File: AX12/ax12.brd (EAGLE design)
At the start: 36.8 x 40.3 mm, 14 parts

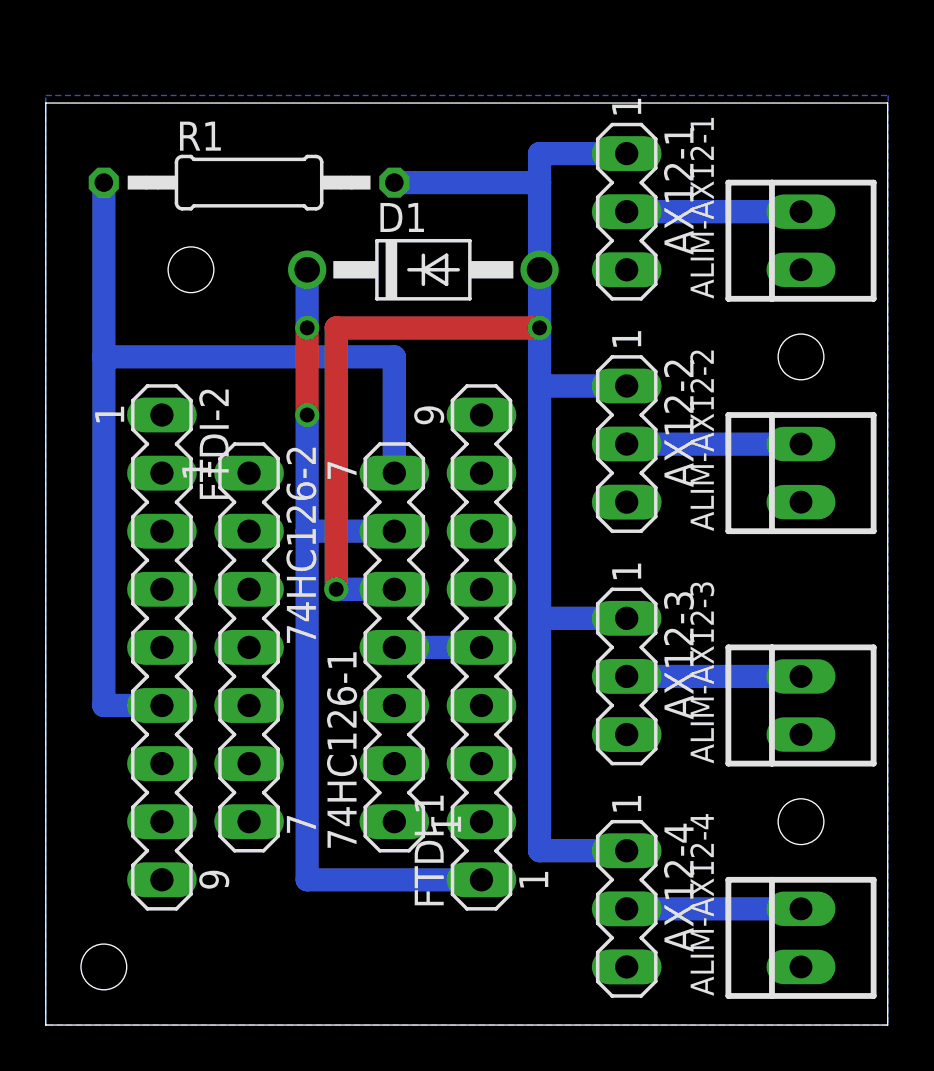
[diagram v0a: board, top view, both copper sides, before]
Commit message: lidar + reset mbed + trou ax12
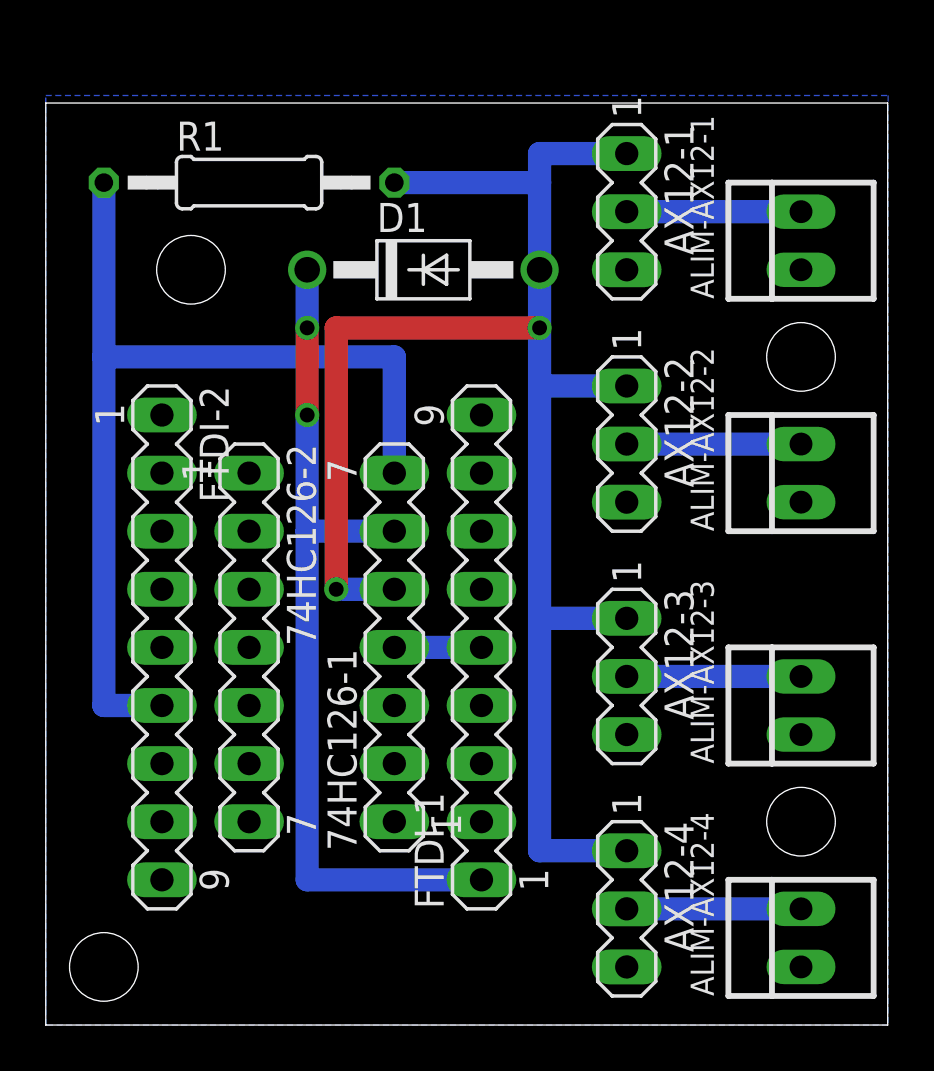
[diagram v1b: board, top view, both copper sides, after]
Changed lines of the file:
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@@
 <wire x1="73.64" y1="60.63" x2="36.83" y2="60.63" width="0" layer="20"/>
 <wire x1="36.83" y1="60.63" x2="36.83" y2="20.32" width="0" layer="20"/>
-<hole x="43.18" y="53.34" drill="2"/>
-<hole x="39.37" y="22.86" drill="2"/>
-<hole x="69.85" y="49.53" drill="2"/>
-<hole x="69.85" y="29.21" drill="2"/>
+<hole x="43.18" y="53.34" drill="3"/>
+<hole x="39.37" y="22.86" drill="3"/>
+<hole x="69.85" y="49.53" drill="3"/>
+<hole x="69.85" y="29.21" drill="3"/>
 </plain>
 <attributes>

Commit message: fix board et gerber file
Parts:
- removed 74HC126-1, 74HC126-2: (no value), con-lstb:MA07-1
- added IC1: (no value), ic-package:DIL14
- moved FTDI-2 1.27 mm to (40.6, 36.8)
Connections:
- net 5V: now also IC1.14; no longer 74HC126-1.7
- net AX12-DATA: now also IC1.12; no longer 74HC126-1.5
- net GND: now also IC1.7; no longer 74HC126-2.7
- net RXD: now also IC1.11; no longer 74HC126-1.4
- net TXD: now also IC1.13; no longer 74HC126-1.6
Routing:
- net 5V: track 43.2 -> 43.9 mm
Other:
- board text added: "USB"
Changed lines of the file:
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@@
 <hole x="69.85" y="49.53" drill="3"/>
 <hole x="69.85" y="29.21" drill="3"/>
+<text x="40.64" y="49.53" size="1.778" layer="1">USB</text>
 </plain>
 <attributes>
@@
 </autorouter>
 <elements>
-<element name="74HC126-1" library="con-lstb" library_urn="urn:adsk.eagle:library:162" package="MA07-1" package3d_urn="urn:adsk.eagle:package:8341/1" value="" x="52.07" y="36.83" smashed="yes" rot="R90">
-<attribute name="MF" value="" x="86.36" y="59.69" size="1.778" layer="27" rot="R90" display="off"/>
-<attribute name="MPN" value="" x="86.36" y="59.69" size="1.778" layer="27" rot="R90" display="off"/>
-<attribute name="NAME" x="50.419" y="27.94" size="1.27" layer="25" ratio="10" rot="R90"/>
-<attribute name="OC_FARNELL" value="unknown" x="86.36" y="59.69" size="1.778" layer="27" rot="R90" display="off"/>
-<attribute name="OC_NEWARK" value="unknown" x="86.36" y="59.69" size="1.778" layer="27" rot="R90" display="off"/>
-<attribute name="VALUE" x="54.991" y="34.29" size="1.27" layer="27" ratio="10" rot="R90"/>
-</element>
 <element name="ALIM-AX12-1" library="con-molex" library_urn="urn:adsk.eagle:library:165" package="22-23-2021" value="22-23-2021" x="69.85" y="54.61" smashed="yes" rot="R90">
 <attribute name="MF" value="MOLEX" x="76.2" y="74.93" size="1.778" layer="27" rot="R90" display="off"/>
@@
 <attribute name="VALUE" x="58.801" y="36.83" size="1.27" layer="27" ratio="10" rot="R90"/>
 </element>
-<element name="FTDI-2" library="con-lstb" library_urn="urn:adsk.eagle:library:162" package="MA09-1" package3d_urn="urn:adsk.eagle:package:8350/1" value="" x="41.91" y="36.83" smashed="yes" rot="R270">
-<attribute name="MF" value="" x="15.24" y="11.43" size="1.778" layer="27" rot="R270" display="off"/>
-<attribute name="MPN" value="" x="15.24" y="11.43" size="1.778" layer="27" rot="R270" display="off"/>
-<attribute name="NAME" x="43.561" y="48.26" size="1.27" layer="25" ratio="10" rot="R270"/>
-<attribute name="OC_FARNELL" value="unknown" x="15.24" y="11.43" size="1.778" layer="27" rot="R270" display="off"/>
-<attribute name="OC_NEWARK" value="unknown" x="15.24" y="11.43" size="1.778" layer="27" rot="R270" display="off"/>
-<attribute name="VALUE" x="38.989" y="36.83" size="1.27" layer="27" ratio="10" rot="R270"/>
-</element>
-<element name="74HC126-2" library="con-lstb" library_urn="urn:adsk.eagle:library:162" package="MA07-1" package3d_urn="urn:adsk.eagle:package:8341/1" value="" x="45.72" y="36.83" smashed="yes" rot="R270">
-<attribute name="MF" value="" x="11.43" y="-5.08" size="1.778" layer="27" rot="R270" display="off"/>
-<attribute name="MPN" value="" x="11.43" y="-5.08" size="1.778" layer="27" rot="R270" display="off"/>
-<attribute name="NAME" x="47.371" y="45.72" size="1.27" layer="25" ratio="10" rot="R270"/>
-<attribute name="OC_FARNELL" value="unknown" x="11.43" y="-5.08" size="1.778" layer="27" rot="R270" display="off"/>
-<attribute name="OC_NEWARK" value="unknown" x="11.43" y="-5.08" size="1.778" layer="27" rot="R270" display="off"/>
-<attribute name="VALUE" x="42.799" y="39.37" size="1.27" layer="27" ratio="10" rot="R270"/>
+<element name="FTDI-2" library="con-lstb" library_urn="urn:adsk.eagle:library:162" package="MA09-1" package3d_urn="urn:adsk.eagle:package:8350/1" value="" x="40.64" y="36.83" smashed="yes" rot="R270">
+<attribute name="MF" value="" x="13.97" y="11.43" size="1.778" layer="27" rot="R270" display="off"/>
+<attribute name="MPN" value="" x="13.97" y="11.43" size="1.778" layer="27" rot="R270" display="off"/>
+<attribute name="NAME" x="42.291" y="48.26" size="1.27" layer="25" ratio="10" rot="R270"/>
+<attribute name="OC_FARNELL" value="unknown" x="13.97" y="11.43" size="1.778" layer="27" rot="R270" display="off"/>
+<attribute name="OC_NEWARK" value="unknown" x="13.97" y="11.43" size="1.778" layer="27" rot="R270" display="off"/>
+<attribute name="VALUE" x="37.719" y="36.83" size="1.27" layer="27" ratio="10" rot="R270"/>
 </element>
 <element name="R1" library="rcl" library_urn="urn:adsk.eagle:library:334" package="0207/12" package3d_urn="urn:adsk.eagle:package:23489/1" value="10k" x="45.72" y="57.15" smashed="yes">
@@
 <attribute name="VALUE" x="43.434" y="56.4642" size="1.27" layer="27" ratio="10"/>
 </element>
+<element name="IC1" library="ic-package" library_urn="urn:adsk.eagle:library:239" package="DIL14" package3d_urn="urn:adsk.eagle:package:16407/2" value="" x="48.26" y="36.83" smashed="yes" rot="R270">
+<attribute name="NAME" x="45.212" y="46.101" size="1.27" layer="25" ratio="10"/>
+<attribute name="VALUE" x="47.625" y="43.561" size="1.27" layer="27" ratio="10" rot="R270"/>
+</element>
 </elements>
 <signals>
 <signal name="5V">
-<contactref element="74HC126-1" pad="7"/>
 <contactref element="R1" pad="1"/>
 <contactref element="FTDI-2" pad="6"/>
+<wire x1="52.07" y1="49.53" x2="39.37" y2="49.53" width="1.016" layer="16"/>
+<wire x1="39.37" y1="57.15" x2="39.37" y2="49.53" width="1.016" layer="16"/>
+<wire x1="40.64" y1="34.29" x2="38.354" y2="34.29" width="1.016" layer="16"/>
+<wire x1="38.354" y1="34.29" x2="38.354" y2="49.53" width="1.016" layer="16"/>
+<wire x1="38.354" y1="49.53" x2="39.37" y2="49.53" width="1.016" layer="16"/>
+<contactref element="IC1" pad="14"/>
 <wire x1="52.07" y1="44.45" x2="52.07" y2="49.53" width="1.016" layer="16"/>
-<wire x1="52.07" y1="49.53" x2="39.37" y2="49.53" width="1.016" layer="16"/>
-<wire x1="39.37" y1="49.53" x2="39.37" y2="34.29" width="1.016" layer="16"/>
-<wire x1="39.37" y1="34.29" x2="41.91" y2="34.29" width="1.016" layer="16"/>
-<wire x1="39.37" y1="57.15" x2="39.37" y2="49.53" width="1.016" layer="16"/>
 </signal>
 <signal name="GND">
 <contactref element="FTDI-1" pad="7"/>
-<contactref element="74HC126-2" pad="7"/>
 <contactref element="AX12-1" pad="3"/>
 <contactref element="AX12-2" pad="3"/>
@@
 <contactref element="ALIM-AX12-3" pad="1"/>
 <contactref element="ALIM-AX12-4" pad="1"/>
-<wire x1="55.88" y1="41.91" x2="62.23" y2="43.18" width="0" layer="19" extent="1-1"/>
+<contactref element="IC1" pad="7"/>
 </signal>
 <signal name="TXD">
-<contactref element="74HC126-1" pad="6"/>
 <contactref element="D1" pad="C"/>
 <contactref element="FTDI-1" pad="1"/>
-<wire x1="52.07" y1="41.91" x2="48.26" y2="41.91" width="1.016" layer="16"/>
+<wire x1="48.26" y1="46.99" x2="48.26" y2="41.91" width="1.016" layer="16"/>
 <wire x1="48.26" y1="41.91" x2="48.26" y2="26.67" width="1.016" layer="16"/>
 <wire x1="48.26" y1="26.67" x2="55.88" y2="26.67" width="1.016" layer="16"/>
@@
 <wire x1="48.26" y1="50.8" x2="48.26" y2="46.99" width="1.016" layer="1"/>
 <via x="48.26" y="46.99" extent="1-16" drill="0.65"/>
-<wire x1="48.26" y1="46.99" x2="48.26" y2="41.91" width="1.016" layer="16"/>
+<contactref element="IC1" pad="13"/>
+<wire x1="52.07" y1="41.91" x2="48.26" y2="41.91" width="1.016" layer="16"/>
 </signal>
 <signal name="RXD">
 <contactref element="FTDI-1" pad="5"/>
-<contactref element="74HC126-1" pad="4"/>
+<contactref element="IC1" pad="11"/>
 <wire x1="52.07" y1="36.83" x2="55.88" y2="36.83" width="1.016" layer="16"/>
 </signal>
 <signal name="AX12-DATA">
-<contactref element="74HC126-1" pad="5"/>
 <contactref element="D1" pad="A"/>
 <contactref element="R1" pad="2"/>
@@
 <wire x1="49.53" y1="50.8" x2="49.53" y2="39.37" width="1.016" layer="1"/>
 <via x="49.53" y="39.37" extent="1-16" drill="0.65"/>
-<wire x1="49.53" y1="39.37" x2="52.07" y2="39.37" width="1.016" layer="16"/>
 <contactref element="AX12-1" pad="1"/>
 <contactref element="AX12-2" pad="1"/>
@@
 <wire x1="62.23" y1="58.42" x2="58.42" y2="58.42" width="1.016" layer="16"/>
 <wire x1="58.42" y1="58.42" x2="58.42" y2="57.15" width="1.016" layer="16"/>
+<contactref element="IC1" pad="12"/>
+<wire x1="52.07" y1="39.37" x2="49.53" y2="39.37" width="1.016" layer="16"/>
 </signal>
 <signal name="N$1">
